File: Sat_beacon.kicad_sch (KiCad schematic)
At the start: 78 parts, among them IC1 LMX2581ESQE_NOPB, J1 Conn_01x03_Pin, J2 Conn_01x05_Pin, J3 Conn_01x03_Pin, J4 Conn_01x02_Pin, Q1 BC817-40, Q2 BC817-40, Q3 BC817-40, SW1 SW_Omron_B3FS, SW2 SW_Omron_B3FS, SW3 SW_Omron_B3FS, SW4 SW_Omron_B3FS, SW5 SW_Omron_B3FS, U1 STM32C011F6Px, U2 LD1117V33, U3 MCP1700x-330xxMB, Y1 FT2MHUPM10.0-T1

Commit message: RF balun added
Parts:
- removed J1: Conn_01x03_Pin, Connector_PinHeader_2.54mm:PinHeader_1x03_P2.54mm_Vertical, symbol Connector:Conn_01x03_Pin
- removed J4: Conn_01x02_Pin, Connector_PinHeader_2.54mm:PinHeader_1x02_P2.54mm_Vertical, symbol Connector:Conn_01x02_Pin
- removed SW1: SW_Omron_B3FS, Button_Switch_SMD:SW_SPST_Omron_B3FS-105xP, symbol Switch:SW_Omron_B3FS
- added C40, C44, C46, C48, C49, C51, C52: 100n, Capacitor_SMD:C_0603_1608Metric, symbol Device:C
- added C41: 5n6, Capacitor_SMD:C_0603_1608Metric, symbol Device:C
- added C42, C45, C50, C59, C60: 4.7u, Capacitor_SMD:C_0805_2012Metric, symbol Device:C
- added C43: 33n, Capacitor_SMD:C_0603_1608Metric, symbol Device:C
- added C47: DNP, Capacitor_SMD:C_0603_1608Metric, symbol Device:C
- added C53, C55: 22u, Capacitor_SMD:C_0603_1608Metric, symbol Device:C
- added C54, C56: 10u, Capacitor_SMD:C_0603_1608Metric, symbol Device:C
- added C57, C58: 2.2u, Capacitor_SMD:C_0603_1608Metric, symbol Device:C
- added C61, C62, C63, C64, C65, C66, C67, C68: 100p, Capacitor_SMD:C_0603_1608Metric, symbol Device:C
- added D4: RF-TGB190TS-CA-P1, LED_SMD:LED_0603_1608Metric, symbol Device:LED
- added IC2: LMX2581ESQE_NOPB, PLL_TI:QFN50P500X500X80-33M, symbol PLL_TI:LMX2581ESQE_NOPB
- added L1, L2, L3, L4: 18n, Inductor_SMD:L_0603_1608Metric, symbol Device:L
- added Q4: BC817-40, Package_TO_SOT_SMD:SOT-23, symbol Transistor_BJT:BC817
- added R20: 560, Resistor_SMD:R_0603_1608Metric, symbol Device:R
- added R21: 0R, Resistor_SMD:R_0603_1608Metric, symbol Device:R
- added R22: 51, Resistor_SMD:R_0805_2012Metric, symbol Device:R
- added R23: 220k, Resistor_SMD:R_0805_2012Metric, symbol Device:R
- added R24: 560, Resistor_SMD:R_1206_3216Metric, symbol Device:R
- added R25, R26: 1k, Resistor_SMD:R_0603_1608Metric, symbol Device:R
- added U4, U5: 1720BL15B0050002E, RF_Converter:Balun_Johanson_0896BM15A0001, symbol 1720BL15B0050002E:1720BL15B0050002E
- R5: value 1k -> 560
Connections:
- net CLK_10MHZ: now also C48.2, R22.1
- net GND: now also C40.1, C41.1, C42.1, C44.1, C45.1, C46.1, C47.1, C49.1, C50.1, C51.1, C52.1, C53.1, C54.1, C55.1, C56.1, C57.1, C58.1, C59.1, C60.1, C61.2, C65.2, C67.2, C68.2, IC2.18 (GND_3), IC2.21 (GND_4), IC2.27 (GND_5), IC2.31 (GND_6), IC2.33 (GND_7), IC2.8 (GND_1), IC2.9 (GND_2), Q4.2 (E), R20.1, R22.2, U4.2, U4.5, U5.2, U5.5; no longer R5.1
- net PLL_CE_2: now also IC2.4 (CE)
- net PLL_CLK_2: now also IC2.1 (CLK)
- net PLL_DATA_2: now also IC2.2 (DATA)
- net PLL_LE_2: now also R5.1, IC2.3 (LE)
- net VCC_D: now also C24.2, R5.2, C40.2, C42.2, C44.2, C45.2, C46.2, C49.2, C50.2, C52.2, C60.2, C61.1, C65.1, C67.1, C68.1, D4.2 (A), IC2.10 (VCCPLL), IC2.16 (VCCBUF), IC2.28 (VCCDIG), IC2.32 (VCCFRAC), IC2.6 (VCCCP), L1.2, L2.1, L3.2, L4.1, R25.1, R26.1
- net VCC_VCO: now also C51.2, C59.2, IC2.17 (VCCVCO)
- net RF1_DC_P: now reaches IC1.14 (RFOUTB+)
- net RF1_DC_P: now also C62.1, L1.1
- net RF1_DC_N: now reaches IC1.15 (RFOUTB-)
- net RF1_DC_N: now also C63.1, L2.2
- net BUFEN: no longer names the net of IC1.26 (BUFEN)
- net BUFEN: now also R26.2
- net LD renamed LD_1
- new net: C47.2, IC2.11 (FIN), R21.1
- new net: C41.2, C43.2, IC2.7 (CPOUT), R21.2
- new net: Q4.1 (B), R23.2
- new net: C58.2, IC2.19 (VBIASVCO)
- new net: C57.2, IC2.22 (VREFVCO)
- new net: C55.2, C56.2, IC2.23 (VBIASCOMP)
- new net: C53.2, C54.2, IC2.24 (VREGVCO)
- new net: IC2.26 (BUFEN), R25.2
- new net: C48.1, IC2.29 (OSCIN)
- new net: D4.1 (K), R24.1
- new net: Q4.3 (C), R24.2
- new net: C43.1, R20.2
- new net LD_2: IC2.25 (LD), R23.1
- new net RF1: U4.1 (UNBAL)
- new net RF1_N: C63.2, U4.4 (BAL_B)
- new net RF1_P: C62.2, U4.3 (BAL_A)
- new net RF2: U5.1 (UNBAL)
- new net RF2_DC_N: C66.1, IC2.15 (RFOUTB-), L4.2
- new net RF2_DC_P: C64.1, IC2.14 (RFOUTB+), L3.1
- new net RF2_N: C66.2, U5.4 (BAL_B)
- new net RF2_P: C64.2, U5.3 (BAL_A)
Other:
- moved on the sheet: C10, C11, C12, C13, C14, C15, C16, C17, C18, C19, C20, C21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

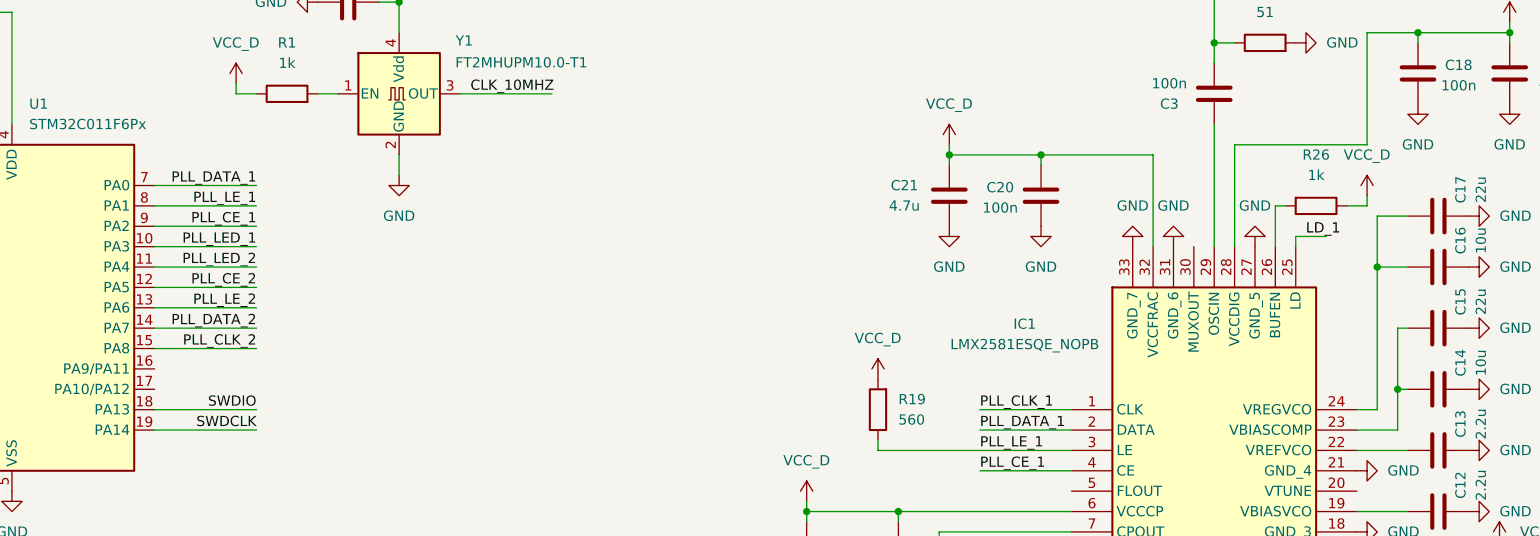
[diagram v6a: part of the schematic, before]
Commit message: PLL RF enable added
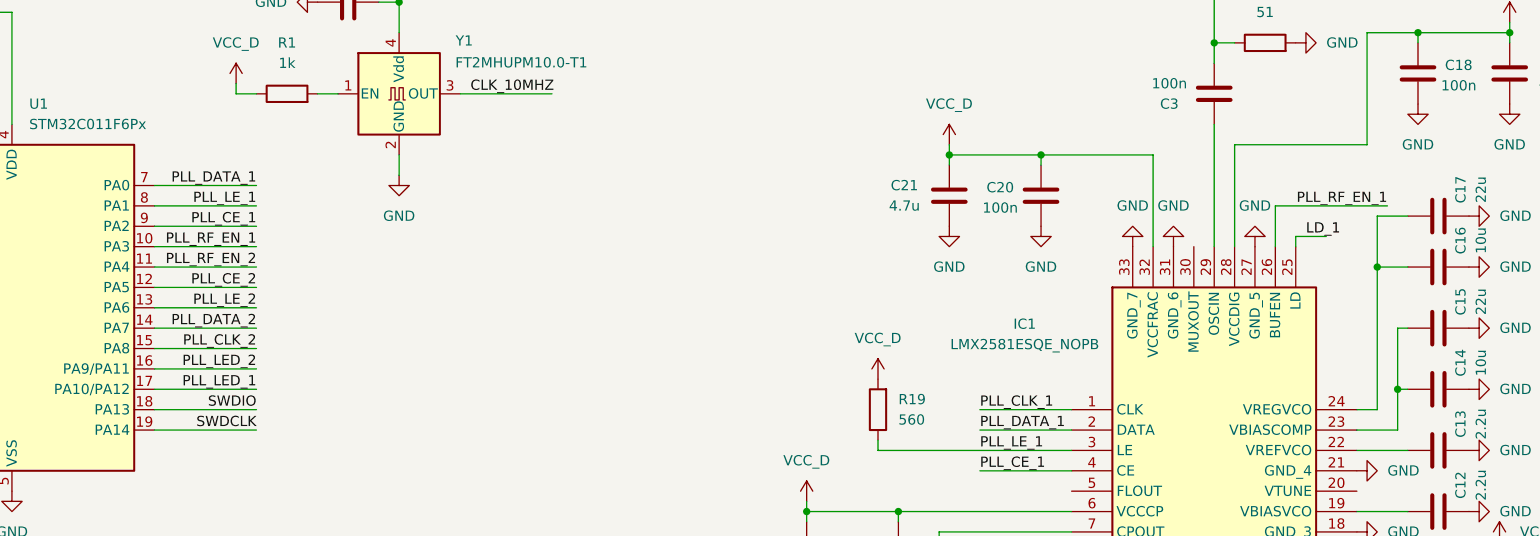
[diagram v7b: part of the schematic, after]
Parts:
- removed R26: 1k, Resistor_SMD:R_0603_1608Metric, symbol Device:R
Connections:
- net PLL_LED_1: now also U1.17 (PA10/PA12); no longer U1.10 (PA3)
- net PLL_LED_2: now also U1.16 (PA9/PA11); no longer U1.11 (PA4)
- net PLL_RF_EN_1: now reaches IC1.26 (BUFEN)
- net PLL_RF_EN_1: now also U1.10 (PA3)
- new net PLL_RF_EN_2: U1.11 (PA4)
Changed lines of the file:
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@@
 	(wire
 		(pts
+			(xy 66.04 67.31) (xy 78.74 67.31)
+		)
+		(stroke
+			(width 0)
+			(type default)
+		)
+	)
+	(wire
+		(pts
 			(xy 40.64 120.65) (xy 38.1 120.65)
 		)
@@
 	(wire
 		(pts
-			(xy 214.63 59.69) (xy 217.17 59.69)
-		)
-		(stroke
-			(width 0)
-			(type default)
-		)
-	)
-	(wire
-		(pts
 			(xy 290.83 99.06) (xy 279.4 99.06)
 		)
@@
 	(wire
 		(pts
-			(xy 66.04 64.77) (xy 78.74 64.77)
-		)
-		(stroke
-			(width 0)
-			(type default)
-		)
-	)
-	(wire
-		(pts
 			(xy 66.04 85.09) (xy 78.74 85.09)
 		)
@@
 	(wire
 		(pts
-			(xy 66.04 67.31) (xy 78.74 67.31)
-		)
-		(stroke
-			(width 0)
-			(type default)
-		)
-	)
-	(wire
-		(pts
 			(xy 426.72 116.84) (xy 426.72 119.38)
 		)
@@
 	(wire
 		(pts
-			(xy 207.01 59.69) (xy 205.74 59.69)
+			(xy 205.74 59.69) (xy 219.71 59.69)
 		)
 		(stroke
@@
 	(wire
 		(pts
+			(xy 66.04 80.01) (xy 78.74 80.01)
+		)
+		(stroke
+			(width 0)
+			(type default)
+		)
+	)
+	(wire
+		(pts
 			(xy 365.76 102.87) (xy 365.76 104.14)
 		)
@@
 	(wire
 		(pts
+			(xy 66.04 64.77) (xy 78.74 64.77)
+		)
+		(stroke
+			(width 0)
+			(type default)
+		)
+	)
+	(wire
+		(pts
 			(xy 203.2 123.19) (xy 203.2 133.35)
 		)
@@
 	(wire
 		(pts
+			(xy 66.04 82.55) (xy 78.74 82.55)
+		)
+		(stroke
+			(width 0)
+			(type default)
+		)
+	)
+	(wire
+		(pts
 			(xy 349.25 134.62) (xy 349.25 135.89)
 		)
@@
 	(wire
 		(pts
-			(xy 217.17 59.69) (xy 217.17 58.42)
-		)
-		(stroke
-			(width 0)
-			(type default)
-		)
-	)
-	(wire
-		(pts
 			(xy 205.74 133.35) (xy 205.74 134.62)
 		)
@@
 		)
 	)
+	(label "PLL_RF_EN_1"
+		(at 78.74 64.77 180)
+		(effects
+			(font
+				(size 1.27 1.27)
+			)
+			(justify right bottom)
+		)
+	)
 	(label "SWDCLK"
 		(at 73.66 191.77 0)
@@
 		)
 	)
-	(label "PLL_LED_1"
-		(at 78.74 64.77 180)
-		(effects
-			(font
-				(size 1.27 1.27)
-			)
-			(justify right bottom)
-		)
-	)
 	(label "PLL_DATA_2"
 		(at 78.74 74.93 180)
@@
 		)
 	)
+	(label "PLL_RF_EN_2"
+		(at 78.74 67.31 180)
+		(effects
+			(font
+				(size 1.27 1.27)
+			)
+			(justify right bottom)
+		)
+	)
 	(label "PLL_CLK"
 		(at 38.1 184.15 0)
@@
 		)
 	)
-	(label "PLL_LED_2"
-		(at 78.74 67.31 180)
-		(effects
-			(font
-				(size 1.27 1.27)
-			)
-			(justify right bottom)
-		)
-	)
 	(label "RF2_N"
 		(at 318.77 217.17 0)
@@
 		)
 	)
+	(label "PLL_LED_2"
+		(at 78.74 80.01 180)
+		(effects
+			(font
+				(size 1.27 1.27)
+			)
+			(justify right bottom)
+		)
+	)
+	(label "PLL_LED_1"
+		(at 78.74 82.55 180)
+		(effects
+			(font
+				(size 1.27 1.27)
+			)
+			(justify right bottom)
+		)
+	)
 	(label "SWDCLK"
 		(at 78.74 87.63 180)
@@
 		)
 	)
+	(label "PLL_RF_EN_1"
+		(at 219.71 59.69 180)
+		(effects
+			(font
+				(size 1.27 1.27)
+			)
+			(justify right bottom)
+		)
+	)
 	(label "PLL_DATA_1"
 		(at 78.74 57.15 180)
@@
 	)
 	(symbol
-		(lib_id "power:VCC")
-		(at 217.17 58.42 0)
-		(mirror y)
-		(unit 1)
-		(exclude_from_sim no)
-		(in_bom yes)
-		(on_board yes)
-		(dnp no)
-		(fields_autoplaced yes)
-		(property "Reference" "#PWR0122"
-			(at 217.17 62.23 0)
-			(effects
-				(font
-					(size 1.27 1.27)
-				)
-				(hide yes)
-			)
-		)
-		(property "Value" "VCC_D"
-			(at 217.17 53.34 0)
-			(effects
-				(font
-					(size 1.27 1.27)
-				)
-			)
-		)
-		(property "Footprint" ""
-			(at 217.17 58.42 0)
-			(effects
-				(font
-					(size 1.27 1.27)
-				)
-				(hide yes)
-			)
-		)
-		(property "Datasheet" ""
-			(at 217.17 58.42 0)
-			(effects
-				(font
-					(size 1.27 1.27)
-				)
-				(hide yes)
-			)
-		)
-		(property "Description" "Power symbol creates a global label with name \"VCC\""
-			(at 217.17 58.42 0)
-			(effects
-				(font
-					(size 1.27 1.27)
-				)
-				(hide yes)
-			)
-		)
-		(pin "1"
-		)
-		(instances
-			(project "Sat_beacon"
-				(path "/d50b57a8-fbd1-4b9f-a519-640b54fbccac"
-					(reference "#PWR0122")
-					(unit 1)
-				)
-			)
-		)
-	)
-	(symbol
 		(lib_id "Device:C")
 		(at 38.1 125.73 180)
@@
 					(unit 1)
 				)
-			)
-		)
-	)
-	(symbol
-		(lib_id "Device:R")
-		(at 210.82 59.69 270)
-		(unit 1)
-		(exclude_from_sim no)
-		(in_bom yes)
-		(on_board yes)
-		(dnp no)
-		(fields_autoplaced yes)
-		(property "Reference" "R26"
-			(at 210.82 53.34 90)
-			(effects
-				(font
-					(size 1.27 1.27)
-				)
-			)
-		)
-		(property "Value" "1k"
-			(at 210.82 55.88 90)
-			(effects
-				(font
-					(size 1.27 1.27)
-				)
-			)
-		)
-		(property "Footprint" "Resistor_SMD:R_0603_1608Metric"
-			(at 210.82 57.912 90)
-			(effects
-				(font
-					(size 1.27 1.27)
-				)
-				(hide yes)
-			)
-		)
-		(property "Datasheet" "~"
-			(at 210.82 59.69 0)
-			(effects
-				(font
-					(size 1.27 1.27)
-				)
-				(hide yes)
-			)
-		)
-		(property "Description" "Resistor"
-			(at 210.82 59.69 0)
-			(effects
-				(font
-					(size 1.27 1.27)
-				)
-				(hide yes)
-			)
-		)
-		(pin "1"
-		)
-		(pin "2"
-		)
-		(instances
-			(project "Sat_beacon"
-				(path "/d50b57a8-fbd1-4b9f-a519-640b54fbccac"
-					(reference "R26")
-					(unit 1)
-				)

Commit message: Fixed VTUNE, added battery, power switch, RF caps, net labels
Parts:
- removed R25: 1k, Resistor_SMD:R_0603_1608Metric, symbol Device:R
- added BT1: 18650, Battery:BatteryHolder_Keystone_1042_1x18650, symbol Device:Battery_Cell
- added J1: Conn_01x05_Pin, Connector_PinHeader_2.54mm:PinHeader_1x05_P2.54mm_Vertical, symbol Connector:Conn_01x05_Pin
- added J4, J5: MMCX, Connector_Coaxial:MMCX_Molex_73415-0961_Horizontal_0.8mm-PCB, symbol Connector:Conn_Coaxial
- added SW1: SW_SPDT_312, symbol Switch:SW_SPDT_312
- C27, C47, R10: now not fitted
- C61, C62, C63, C64, C65, C66, C67, C68: footprint Capacitor_SMD:C_0603_1608Metric -> Capacitor_SMD:C_0402_1005Metric
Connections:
- net PLL_CE is gone; now on net PLL_CE_1: J2.5 (Pin_5)
- net PLL_CLK is gone; now on net PLL_CLK_1: J2.2 (Pin_2)
- net PLL_DATA is gone; now on net PLL_DATA_1: J2.3 (Pin_3)
- net PLL_LE is gone; now on net PLL_LE_1: J2.4 (Pin_4)
- net +BATT: now also BT1.1 (+); no longer C28.2, C29.2, C32.2, C33.2, U2.3 (VI), U3.2 (VI)
- net GND: now also C64.2, BT1.2 (-), J1.1 (Pin_1), J4.2 (Ext), J5.2 (Ext); no longer C67.2
- net PLL_CE_2: now also J1.5 (Pin_5)
- net PLL_CLK_2: now also J1.2 (Pin_2)
- net PLL_DATA_2: now also J1.3 (Pin_3)
- net PLL_LE_2: now also J1.4 (Pin_4)
- net PLL_RF_EN_2: now also IC2.26 (BUFEN)
- net RF1: now also J4.1 (In)
- net RF2: now also J5.1 (In)
- net RF2_DC_N: now also C67.1; no longer C66.1
- net RF2_DC_P: now also C66.1; no longer C64.1
- net RF2_N: now also C67.2; no longer C66.2
- net RF2_P: now also C66.2; no longer C64.2
- net VCC_D: now also C64.1; no longer C67.1
- net VTUNE_2: now reaches C47.2, R21.1
- net VTUNE_2: now also IC2.20 (VTUNE); no longer IC2.11 (FIN)
- net VTUNE_1: now reaches C27.2, R7.1
- net VTUNE_1: now also IC1.20 (VTUNE); no longer IC1.11 (FIN)
- new net: C28.2, C29.2, C32.2, C33.2, SW1.1 (B), U2.3 (VI), U3.2 (VI)
- new net VCC_CHARGER: SW1.3 (A)
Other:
- moved on the sheet: C1, C2, C25, C26, C41, C43, C61, J3, L1, L2, L3, L4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
